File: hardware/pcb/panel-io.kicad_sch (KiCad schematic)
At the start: 0 parts

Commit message: Capture the panel-io sheet
46 components over 59 placements: both ribbon buses with their series/filter
networks, the three 74HC14 debounce channels, RGB, both comms ports, the
expansion header and the two sensor inputs.

ERC has no errors and the dangling-global count falls 33 -> 4. The four left are
AUDIO_IN_L/R and AUDIO_OUT_L/R, waiting on the audio sheet. That number was
predicted before the sheet was drawn, so it landing exactly is the check rather
than a coincidence.

Pin-map enforcement was run by script against pins.yaml. The first attempt
reported 20 of 29 pins failing, which was the check being naive rather than the
schematic being wrong -- every bus pin reaches its connector THROUGH the series
resistor the spec mandates. Redone as a reachability walk through R, C and the
debouncer: all 29 pins that declare a connector reach it, and A10/A11 reach none
because they are on-board measurements.

Two things verified rather than assumed. The transposition trap is the right way
round: R46 is 10k on A4 (FSR), R45 is 3k on A5 (soft pot). And D13/D14 carry J15
as well as the debouncer -- which reads like an error until you remember comms
port B and SW1/SW2 are alternatives on the same pins. D7 is not shared, which is
the whole reason loa's hook switch is on SW3.

C is a population choice per channel: 220n on SW1/SW2, 1u on SW3 for a hook
lever. The four optional resistors -- both I2C pull-ups and both sensor
pulldowns -- carry the DNP flag.
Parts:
- added C10, C11, C12, C13, C14, C15, C16, C17, C18: 100n, Capacitor_SMD:C_0603_1608Metric, symbol Device:C
- added C19, C20: 220n, Capacitor_SMD:C_0603_1608Metric, symbol Device:C
- added C21: 1u, Capacitor_SMD:C_0603_1608Metric, symbol Device:C
- added J10: FSR, Connector_JST:JST_XH_B2B-XH-A_1x02_P2.50mm_Vertical, symbol Connector_Generic:Conn_01x02
- added J11: Digital bus, Connector_IDC:IDC-Header_2x05_P2.54mm_Vertical, symbol Connector_Generic:Conn_02x05_Odd_Even
- added J12: RGB status, Connector_JST:JST_XH_B4B-XH-A_1x04_P2.50mm_Vertical, symbol Connector_Generic:Conn_01x04
- added J13A: Comms A - Qwiic, Connector_JST:JST_SH_SM04B-SRSS-TB_1x04-1MP_P1.00mm_Horizontal, symbol Connector_Generic:Conn_01x04
- added J13B: Comms A - module, Connector_JST:JST_XH_B6B-XH-A_1x06_P2.50mm_Vertical, symbol Connector_Generic:Conn_01x06
- added J15: Comms B - module, Connector_JST:JST_XH_B6B-XH-A_1x06_P2.50mm_Vertical, symbol Connector_Generic:Conn_01x06
- added J16: Expansion / SPI1, Connector_PinHeader_2.54mm:PinHeader_2x04_P2.54mm_Vertical, symbol Connector_Generic:Conn_02x04_Odd_Even
- added J5: Analogue bus, Connector_IDC:IDC-Header_2x05_P2.54mm_Vertical, symbol Connector_Generic:Conn_02x05_Odd_Even
- added J6: SW1 switch, Connector_JST:JST_XH_B2B-XH-A_1x02_P2.50mm_Vertical, symbol Connector_Generic:Conn_01x02
- added J7: SW2 switch, Connector_JST:JST_XH_B2B-XH-A_1x02_P2.50mm_Vertical, symbol Connector_Generic:Conn_01x02
- added J8: SW3 switch, Connector_JST:JST_XH_B2B-XH-A_1x02_P2.50mm_Vertical, symbol Connector_Generic:Conn_01x02
- added J9: Soft pot, Connector_JST:JST_XH_B3B-XH-A_1x03_P2.50mm_Vertical, symbol Connector_Generic:Conn_01x03
- added R19, R20, R21, R22, R23, R24, R25, R26: 1k, Resistor_SMD:R_0603_1608Metric, symbol Device:R
- added R27, R28, R29, R30, R31, R32, R33: 100R, Resistor_SMD:R_0603_1608Metric, symbol Device:R
- added R34, R35, R36, R37, R38, R39, R46: 10k, Resistor_SMD:R_0603_1608Metric, symbol Device:R
- added R40: 510, Resistor_SMD:R_0603_1608Metric, symbol Device:R
- added R41, R42: 300, Resistor_SMD:R_0603_1608Metric, symbol Device:R
- added R43, R44: 4k7, Resistor_SMD:R_0603_1608Metric, symbol Device:R
- added R45: 3k, Resistor_SMD:R_0603_1608Metric, symbol Device:R
- added U3: 74HC14, Package_SO:SOIC-14_3.9x8.7mm_P1.27mm, symbol 74xx:74HC14
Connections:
- new net +3V3: C18.1, J11.1 (Pin_1), J13A.2 (Pin_2), J13B.2 (Pin_2), J15.2 (Pin_2), J16.2 (Pin_2), R34.1, R36.1, R38.1, R43.1, R44.1, U3.14 (VCC)
- new net +3V3A: J10.1 (Pin_1), J5.1 (Pin_1), J9.1 (Pin_1)
- new net +5V: J12.1 (Pin_1), J13B.1 (Pin_1), J15.1 (Pin_1), J16.1 (Pin_1)
- new net A0: C10.1, R19.2
- new net A0_W: J5.2 (Pin_2), R19.1
- new net A1: C11.1, R20.2
- new net A1_W: J5.3 (Pin_3), R20.1
- new net A2: C12.1, R21.2
- new net A2_W: J5.4 (Pin_4), R21.1
- new net A3: C13.1, R22.2
- new net A3_W: J5.5 (Pin_5), R22.1
- new net A4: J10.2 (Pin_2), R46.1
- new net A5: J9.2 (Pin_2), R45.1
- new net A6: C14.1, R23.2
- new net A6_W: J5.6 (Pin_6), R23.1
- new net A7: C15.1, R24.2
- new net A7_W: J5.7 (Pin_7), R24.1
- new net A8: C16.1, R25.2
- new net A8_W: J5.8 (Pin_8), R25.1
- new net A9: C17.1, R26.2
- new net A9_W: J5.9 (Pin_9), R26.1
- new net D0: R27.2
- new net D0_S: J11.2 (Pin_2), R27.1
- new net D1: R28.2
- new net D10: J16.7 (Pin_7)
- new net D11: J13A.4 (Pin_4), J13B.4 (Pin_4), R44.2
- new net D12: J13A.3 (Pin_3), J13B.5 (Pin_5), R43.2
- new net D13: J15.4 (Pin_4), U3.4
- new net D14: J15.5 (Pin_5), U3.2
- new net D1_S: J11.3 (Pin_3), R28.1
- new net D2: R29.2
- new net D26: R40.2
- new net D27: R41.2
- new net D29: R42.2
- new net D2_S: J11.4 (Pin_4), R29.1
- new net D3: R30.2
- new net D30: J16.8 (Pin_8)
- new net D3_S: J11.5 (Pin_5), R30.1
- new net D4: R31.2
- new net D4_S: J11.6 (Pin_6), R31.1
- new net D5: R32.2
- new net D5_S: J11.7 (Pin_7), R32.1
- new net D6: R33.2
- new net D6_S: J11.8 (Pin_8), R33.1
- new net D7: U3.6
- new net D8: J16.5 (Pin_5)
- new net D9: J16.6 (Pin_6)
- new net GND: C10.2, C11.2, C12.2, C13.2, C14.2, C15.2, C16.2, C17.2, C18.2, C19.2, C20.2, C21.2, J11.10 (Pin_10), J13A.1 (Pin_1), J13B.3 (Pin_3), J13B.6 (Pin_6), J15.3 (Pin_3), J15.6 (Pin_6), J16.3 (Pin_3), J16.4 (Pin_4), J5.10 (Pin_10), J6.2 (Pin_2), J7.2 (Pin_2), J8.2 (Pin_2), J9.3 (Pin_3), R45.2, R46.2, U3.11, U3.13, U3.7 (GND), U3.9
- new net RGB_B: J12.4 (Pin_4), R42.1
- new net RGB_G: J12.3 (Pin_3), R41.1
- new net RGB_R: J12.2 (Pin_2), R40.1
- new net SW1_F: C19.1, R35.2, U3.1
- new net SW1_RAW: J6.1 (Pin_1), R34.2, R35.1
- new net SW2_F: C20.1, R37.2, U3.3
- new net SW2_RAW: J7.1 (Pin_1), R36.2, R37.1
- new net SW3_F: C21.1, R39.2, U3.5
- new net SW3_RAW: J8.1 (Pin_1), R38.2, R39.1
- no-connect marks 0 -> 4

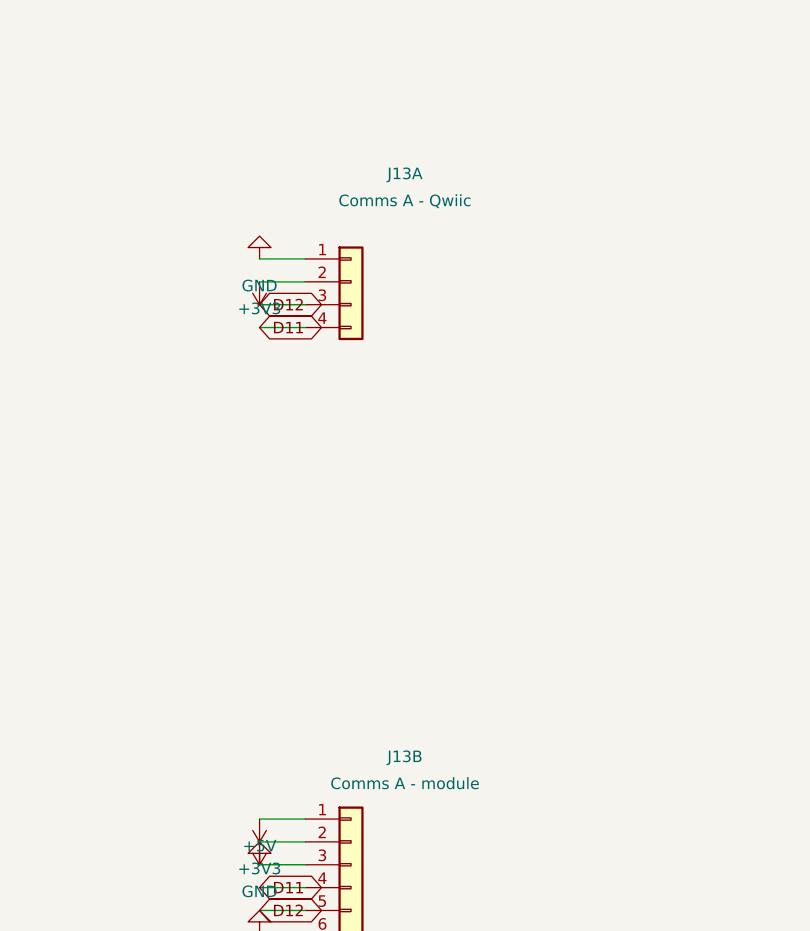
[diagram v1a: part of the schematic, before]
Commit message: Rename J13A -> J13 and J13B -> J19; KiCad will not accept the old names
KiCad parses a reference designator as PREFIX + NUMBER. J13A ends in a
letter, so KiCad read the whole string as a prefix with no number and
considered the symbol UNANNOTATED. One cause, three symptoms, all of
which cost time this week:

  - the BOM exporter emitted "J13A?", which JLC rejected
  - Update PCB from Schematic refuses to run until the sheet is
    annotated
  - accepting the annotation renamed them to J13A1/J13B1, which changed
    the references, broke every footprint path, and made all 131
    components look like additions again -- the loop we were stuck in

There was no way to keep the names; the annotation rules are not
negotiable. J13 keeps the Qwiic socket associated with comms port A on
D11/D12; J19 takes the module port at the end of the numbering.

39 replacements across 16 files: both schematics, the board, seven docs,
three firmware files and the tooling that names them.

TWO THINGS DELIBERATELY NOT REWRITTEN:

  discovery/evidence/  Append-only dated evidence. Rewriting the
                       2026-08-19 snapshot to today names would falsify
                       what JLC actually returned. That is what the
                       ledger rule is for.
  fab_package.py       Its comment explains WHY "J13A?" appeared and
                       needs the old name to make sense. A note records
                       that it is now fixed at source; the reconciliation
                       stays, because it costs nothing and would catch a
                       recurrence.

VERIFIED: no reference anywhere now lacks a numeric suffix, ERC is 0/0,
pinmap.md is current, all 124 footprint paths survived the rename, and
parity still reports exactly the 25 intended changes.

pins.yaml changes only the CONNECTOR column. D11/D12 are untouched, so
the frozen pin map is not violated -- this is a rename, not a repurpose.
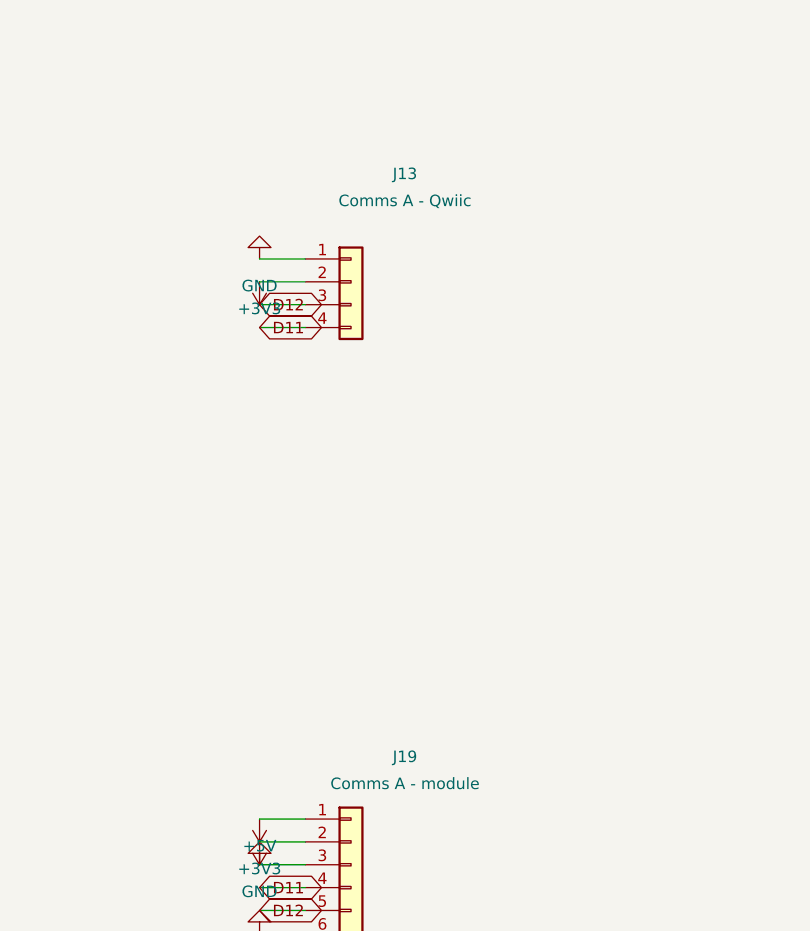
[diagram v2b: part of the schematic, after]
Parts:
- renumbered J13A to J13, J13B to J19
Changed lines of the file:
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@@
 		(on_board yes)
 		(dnp no)
-		(property "Reference" "J13A"
+		(property "Reference" "J13"
 			(at 361.6 137.86 0)
 			(effects
@@
 			(project "caryatid"
 				(path "/49c08c53-8a29-4df2-81cf-05d7b7c47990/810df3d0-2a5c-411d-aa14-77e2cbf45434"
-					(reference "J13A")
+					(reference "J13")
 					(unit 1)
 				)
@@
 		(on_board yes)
 		(dnp no)
-		(property "Reference" "J13B"
+		(property "Reference" "J19"
 			(at 361.6 202.63 0)
 			(effects
@@
 			(project "caryatid"
 				(path "/49c08c53-8a29-4df2-81cf-05d7b7c47990/810df3d0-2a5c-411d-aa14-77e2cbf45434"
-					(reference "J13B")
-					(unit 1)
-				)
+					(reference "J19")
+					(unit 1)
+				)

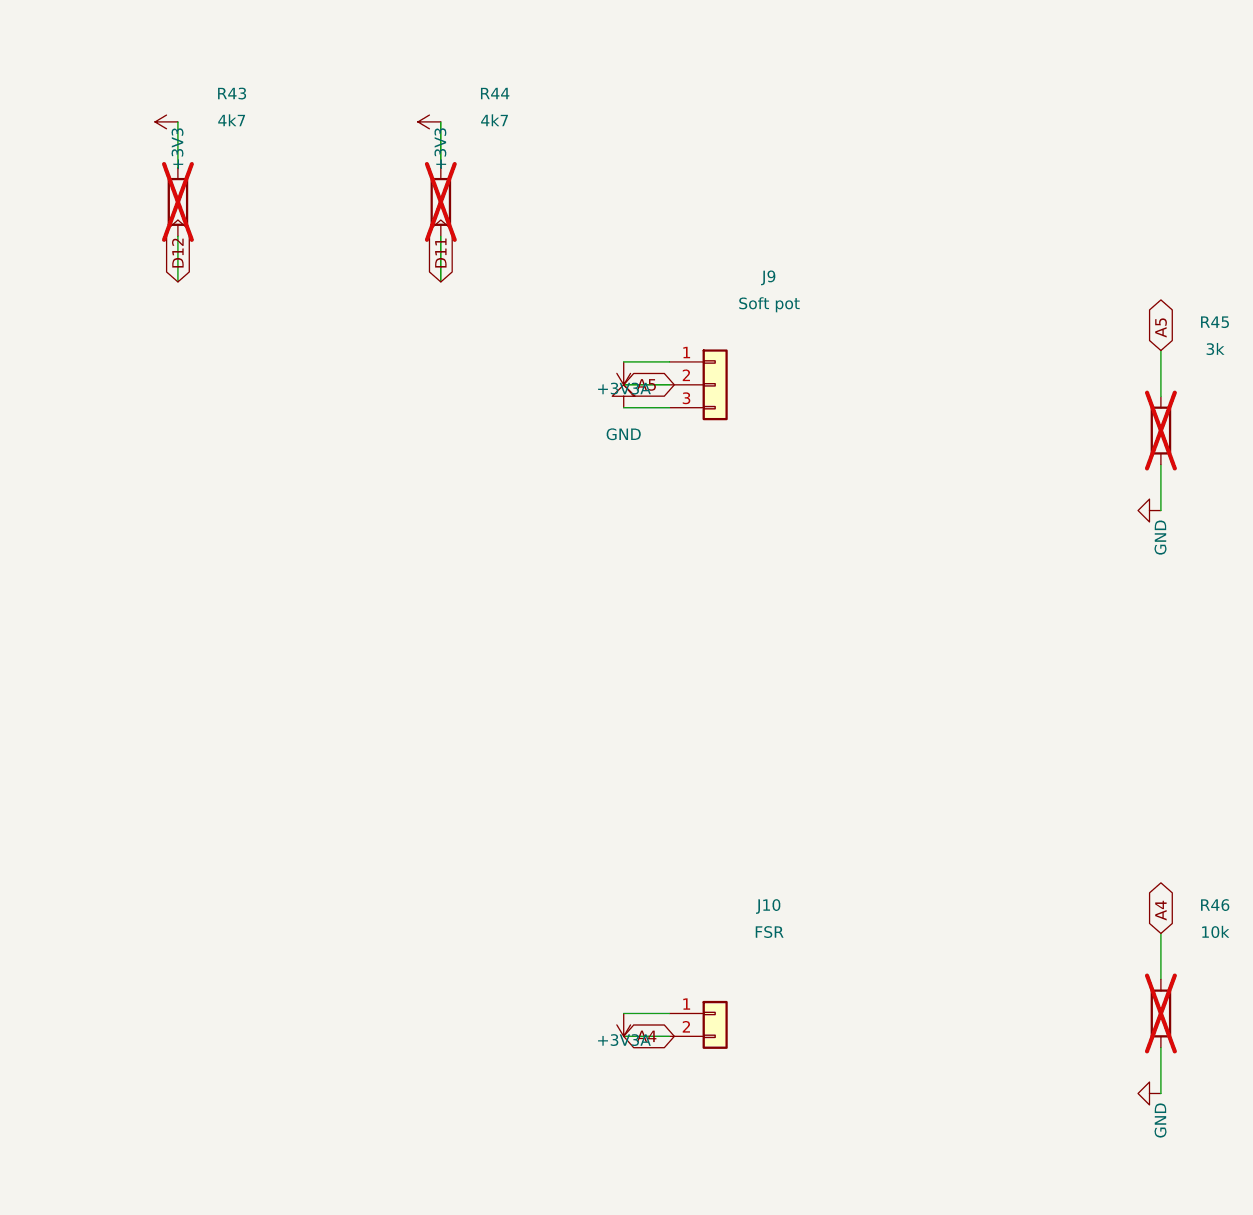
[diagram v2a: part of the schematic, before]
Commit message: ADR 0010 step 1: zero DNP in the schematic; the PCB is NOT yet updated
Three one-shot scripts, run in this order, and the order matters:

  drop_open_positions.py       R48 R50 R64 R66 deleted
  add_right_mic_jumpers.py     JP4/JP5/JP6 + R68, right channel assembled
  populate_panelio_options.py  R43 R44 R45 R46 assembled

R66 HAD TO GO FIRST. It taps AUDIO_IN_R at (439.42, 350.52), which is
downstream of where JP5 lands, so deleting it after the split would have
left the pad on the wrong side of the jumper. add_right_mic_jumpers.py
checks for R66 and refuses to run while it is present.

  JP4  BIAS_E_R / MIC_R / BIAS_C_R        2k2 to 3V3A | off | 220R to 5V
  JP5  AMP_OUT_R / AUDIO_IN_R / BYPASS_R  op-amp | bypass
  JP6  LEG_101_R / GAINLEG_R / LEG_256_R  1k x101 | 392R x256
  R68  392R, the x256 leg, alongside R62 off OPA_R_N

THE MIRROR IS +149.86 mm IN Y, MEASURED NOT CHOSEN. R51/R53, R58/R62,
C25/C29, R63/R65 and C24/C28 all agree, and 149.86 / 1.27 = 118, so the
translation lands every coordinate back on the connection grid. That is
the trap the left-channel run fell into first: round numbers gave 17
endpoint_off_grid warnings, and an off-grid pin is how a connection
silently fails to form.

R68 IS THE ONE PART THAT IS NOT A TRANSLATION. The left has two gain
legs, R58 1k and R67 392R; the right had only R62, because a follower
needs no second leg. Without R68 there is nothing for JP6 to select.

VERIFIED BY NETLIST DIFF, WHICH IS THE REAL CHECK -- ERC does not notice
a jumper wired to the wrong net. 99 of 107 pre-existing nets are
byte-identical, six nets are new, and every one of the eight changes is
intended:

  MIC_R       R53.2 R54.2  ->  JP4.2
  AUDIO_IN_R  C29.2 R65.2 R66.1  ->  JP5.2
  GAINLEG_R   R62.2  ->  JP6.2
  OPA_R_N     + R68.1
  OUT_L_J     - R48.1        OUT_R_J  - R50.1
  BYPASS_L    - R64.1        GND      - four shunt returns

Saved as discovery/evidence/2026-08-21-audio-netlist-diff.txt. ERC is 0
violations at --severity-all after each o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
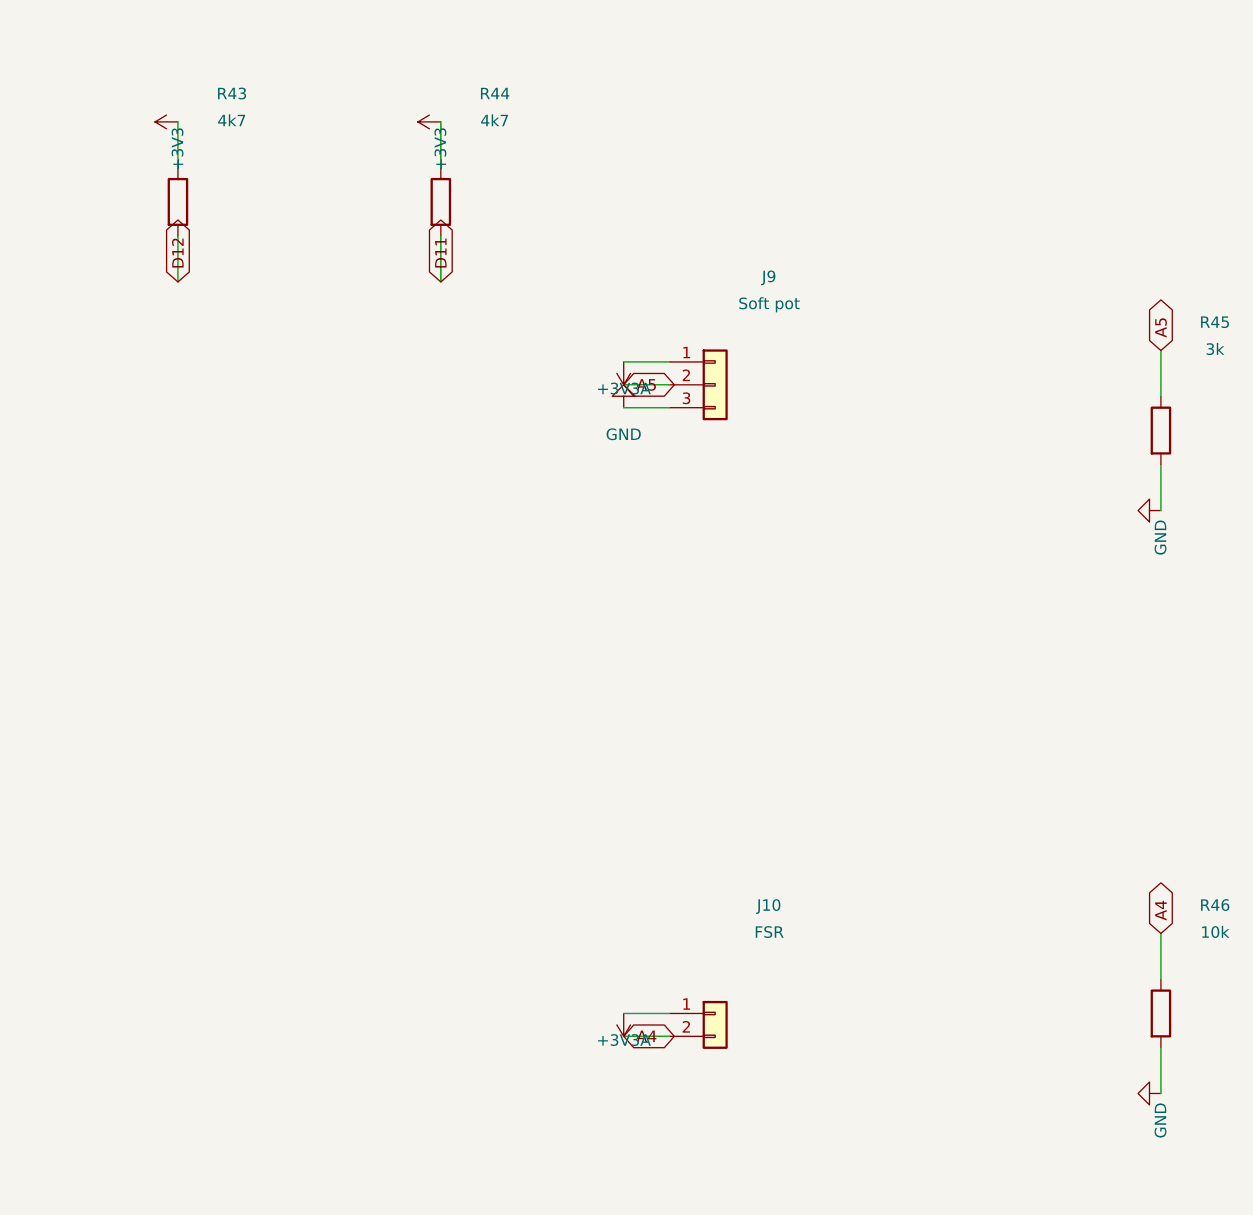
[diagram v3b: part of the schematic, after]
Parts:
- R43, R44, R45, R46: now fitted
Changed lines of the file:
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@@
 		(in_bom yes)
 		(on_board yes)
-		(dnp yes)
+		(dnp no)
 		(property "Reference" "R43"
 			(at 416.21 127.69999999999999 0)
@@
 		(in_bom yes)
 		(on_board yes)
-		(dnp yes)
+		(dnp no)
 		(property "Reference" "R44"
 			(at 445.42 127.69999999999999 0)
@@
 		(in_bom yes)
 		(on_board yes)
-		(dnp yes)
+		(dnp no)
 		(property "Reference" "R45"
 			(at 525.43 153.1 0)
@@
 		(in_bom yes)
 		(on_board yes)
-		(dnp yes)
+		(dnp no)
 		(property "Reference" "R46"
 			(at 525.43 217.87 0)
